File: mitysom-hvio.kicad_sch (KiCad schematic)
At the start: 13 parts, among them J100 Plug_Samtec_SEAM-50-02.0-L-08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, U501 LSF0108RKSR, U502 LSF0108RKSR

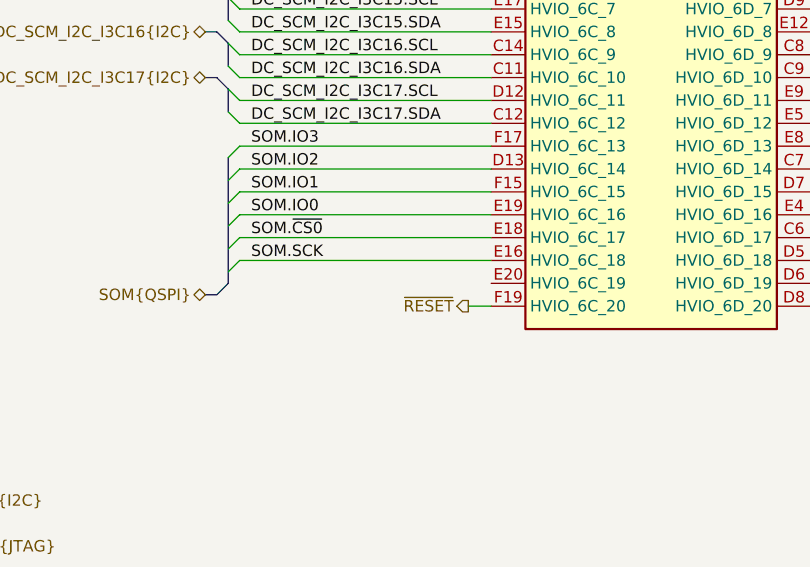
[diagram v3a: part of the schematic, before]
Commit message: [#100282] Connect QSPI_ISO_SW and MCU LEDs signals
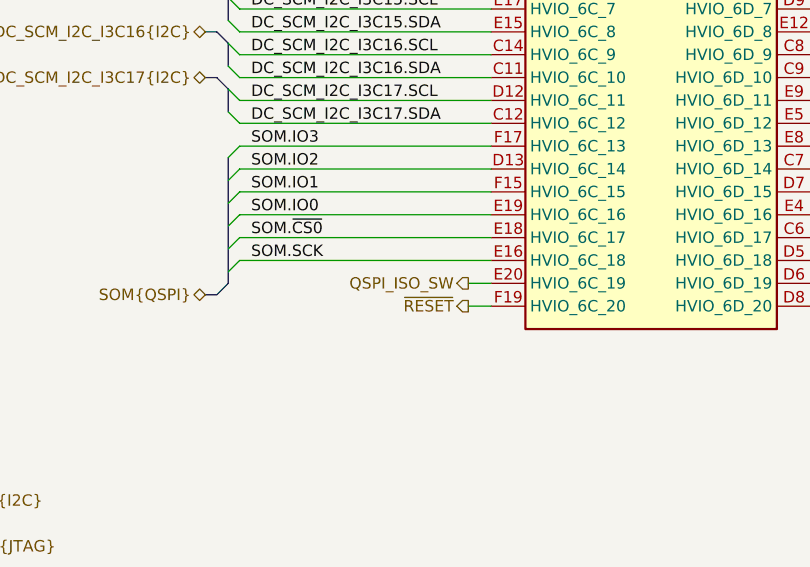
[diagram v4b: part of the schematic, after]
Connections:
- net QSPI_ISO_SW: now reaches J100.E20 (HVIO_6C_19)
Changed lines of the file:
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@@
+	(wire
+		(pts
+			(xy 264.16 186.69) (xy 266.7 186.69)
+		)
+		(stroke
+			(width 0)
+			(type default)
+		)
+	)
 	(wire
 		(pts
@@
 		)
 	)
+	(hierarchical_label "QSPI_ISO_SW"
+		(shape output)
+		(at 264.16 186.69 180)
+		(effects
+			(font
+				(size 1.27 1.27)
+			)
+			(justify right)
+		)
+	)

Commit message: [#100282] WIP: Clear ERC
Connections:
- net at C504.2, R506.2, U502.19 (VREF_{B}): now also U502.20 (EN)
- net at C501.2, R501.2, U501.19 (VREF_{B}): now also U501.20 (EN)
- no-connect marks 8 -> 11
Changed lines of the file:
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@@
 	)
 	(junction
+		(at 99.06 130.81)
+		(diameter 0)
+		(color 0 0 0 0)
+	)
+	(junction
+		(at 356.87 134.62)
+		(diameter 0)
+		(color 0 0 0 0)
+	)
+	(junction
 		(at 359.41 121.92)
 		(diameter 0)
@@
 	)
 	(junction
+		(at 99.06 120.65)
+		(diameter 0)
+		(color 0 0 0 0)
+	)
+	(junction
 		(at 99.06 161.29)
 		(diameter 0)
@@
 	)
 	(no_connect
+		(at 302.26 163.83)
+	)
+	(no_connect
 		(at 96.52 147.32)
 	)
 	(no_connect
+		(at 132.08 60.96)
+	)
+	(no_connect
 		(at 77.47 154.94)
 	)
 	(no_connect
+		(at 132.08 231.14)
+	)
+	(no_connect
 		(at 77.47 152.4)
 	)
@@
 	(wire
 		(pts
+			(xy 99.06 130.81) (xy 99.06 133.35)
+		)
+		(stroke
+			(width 0)
+			(type default)
+		)
+	)
+	(wire
+		(pts
 			(xy 367.03 121.92) (xy 359.41 121.92)
 		)
@@
 	(wire
 		(pts
+			(xy 99.06 120.65) (xy 99.06 130.81)
+		)
+		(stroke
+			(width 0)
+			(type default)
+		)
+	)
+	(wire
+		(pts
 			(xy 356.87 121.92) (xy 356.87 134.62)
 		)
@@
 	(wire
 		(pts
+			(xy 354.33 137.16) (xy 356.87 137.16)
+		)
+		(stroke
+			(width 0)
+			(type default)
+		)
+	)
+	(wire
+		(pts
 			(xy 356.87 165.1) (xy 356.87 167.64)
 		)
@@
 	(wire
 		(pts
+			(xy 356.87 137.16) (xy 356.87 134.62)
+		)
+		(stroke
+			(width 0)
+			(type default)
+		)
+	)
+	(wire
+		(pts
 			(xy 167.64 66.04) (xy 196.85 66.04)
 		)
@@
 	(wire
 		(pts
-			(xy 99.06 118.11) (xy 99.06 130.81)
+			(xy 99.06 118.11) (xy 99.06 120.65)
 		)
 		(stroke
@@
 	(wire
 		(pts
+			(xy 96.52 133.35) (xy 99.06 133.35)
+		)
+		(stroke
+			(width 0)
+			(type default)
+		)
+	)
+	(wire
+		(pts
 			(xy 76.2 118.11) (xy 74.93 118.11)
 		)
@@
 	)
 	(symbol
+		(lib_id "antmicropower:PWR_FLAG")
+		(at 99.06 120.65 90)
+		(unit 1)
+		(body_style 1)
+		(exclude_from_sim no)
+		(in_bom yes)
+		(on_board yes)
+		(in_pos_files yes)
+		(dnp no)
+		(property "Reference" "#FLG0503"
+			(at 97.155 120.65 0)
+			(hide yes)
+			(show_name no)
+			(do_not_autoplace no)
+			(effects
+				(font
+					(size 1.27 1.27)
+				)
+			)
+		)
+		(property "Value" "PWR_FLAG"
+			(at 96.266 120.65 90)
+			(show_name no)
+			(do_not_autoplace no)
+			(effects
+				(font
+					(size 1.27 1.27)
+				)
+				(justify left)
+			)
+		)
+		(property "Footprint" ""
+			(at 99.06 120.65 0)
+			(hide yes)
+			(show_name no)
+			(do_not_autoplace no)
+			(effects
+				(font
+					(size 1.27 1.27)
+				)
+			)
+		)
+		(property "Datasheet" ""
+			(at 99.06 120.65 0)
+			(hide yes)
+			(show_name no)
+			(do_not_autoplace no)
+			(effects
+				(font
+					(size 1.27 1.27)
+				)
+			)
+		)
+		(property "Description" ""
+			(at 101.6 120.65 0)
+			(hide yes)
+			(show_name no)
+			(do_not_autoplace no)
+			(effects
+				(font
+					(size 1.27 1.27)
+				)
+				(justify left bottom)
+			)
+		)
+		(pin "1"
+		)
+		(instances
+			(project "altera-modular-agilex-5-dc-scm"
+				(path "/6bb9d978-a328-4b30-874b-55170a976185/c1ff3762-7815-4072-9586-bdd6f23ff1ef"
+					(reference "#FLG0503")
+					(unit 1)
+				)
+			)
+		)
+	)
+	(symbol
 		(lib_id "antmicropower:GND")
 		(at 356.87 167.64 0)
@@
 	)
 	(symbol
-		(lib_id "power:+1V8")
+		(lib_id "antmicropower:+1V8")
 		(at 101.6 110.49 0)
 		(unit 1)
@@
 		)
 		(property "Footprint" ""
-			(at 101.6 110.49 0)
+			(at 116.84 118.11 0)
 			(hide yes)
 			(show_name no)
@@
 				(font
 					(size 1.27 1.27)
+					(thickness 0.15)
 				)
+				(justify left bottom)
 			)
 		)
 		(property "Datasheet" ""
-			(at 101.6 110.49 0)
+			(at 116.84 120.65 0)
 			(hide yes)
 			(show_name no)
@@
 				(font
 					(size 1.27 1.27)
+					(thickness 0.15)
 				)
+				(justify left bottom)
 			)
 		)
 		(property "Description" "Power symbol creates a global label with name \"+1V8\""
-			(at 101.6 110.49 0)
+			(at 116.84 123.19 0)
+			(hide yes)
+			(show_name no)
+			(do_not_autoplace no)
+			(effects
+				(font
+					(size 1.27 1.27)
+				)
+				(justify left bottom)
+			)
+		)
+		(property "Author" "Antmicro"
+			(at 116.84 115.57 0)
 			(hide yes)
 			(show_name no)
@@
 				(font
 					(size 1.27 1.27)
+					(thickness 0.15)
 				)
+				(justify left bottom)
+			)
+		)
+		(property "License" "Apache-2.0"
+			(at 116.84 118.11 0)
+			(hide yes)
+			(show_name no)
+			(do_not_autoplace no)
+			(effects
+				(font
+					(size 1.27 1.27)
+					(thickness 0.15)
+				)
+				(justify left bottom)
 			)
 		)
@@
 	)
 	(symbol
-		(lib_id "power:+1V8")
+		(lib_id "antmicropower:+1V8")
 		(at 330.2 119.38 0)
 		(unit 1)
@@
 		)
 		(property "Footprint" ""
-			(at 330.2 119.38 0)
+			(at 345.44 127 0)
 			(hide yes)
 			(show_name no)
@@
 				(font
 					(size 1.27 1.27)
+					(thickness 0.15)
 				)
+				(justify left bottom)
 			)
 		)
 		(property "Datasheet" ""
-			(at 330.2 119.38 0)
+			(at 345.44 129.54 0)
 			(hide yes)
 			(show_name no)
@@
 				(font
 					(size 1.27 1.27)
+					(thickness 0.15)
 				)
+				(justify left bottom)
 			)
 		)
 		(property "Description" "Power symbol creates a global label with name \"+1V8\""
-			(at 330.2 119.38 0)
+			(at 345.44 132.08 0)
+			(hide yes)
+			(show_name no)
+			(do_not_autoplace no)
+			(effects
+				(font
+					(size 1.27 1.27)
+				)
+				(justify left bottom)
+			)
+		)
+		(property "Author" "Antmicro"
+			(at 345.44 124.46 0)
 			(hide yes)
 			(show_name no)
@@
 				(font
 					(size 1.27 1.27)
+					(thickness 0.15)
 				)
+				(justify left bottom)
+			)
+		)
+		(property "License" "Apache-2.0"
+			(at 345.44 127 0)
+			(hide yes)
+			(show_name no)
+			(do_not_autoplace no)
+			(effects
+				(font
+					(size 1.27 1.27)
+					(thickness 0.15)
+				)
+				(justify left bottom)
 			)
 		)
